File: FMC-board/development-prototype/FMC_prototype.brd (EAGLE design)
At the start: 103.9 x 69.8 mm, 91 parts, among them J1 PJ-102AH, J2 DC_POWER_JACK-PJ-102AH, U1 TPS79301, U10 ADN4664, U11 ADN4663, U2 TPS79333, U3 ADN4663, U4 ADN4663, U5 ADN4664, U6 PDS1-S12-S5-S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

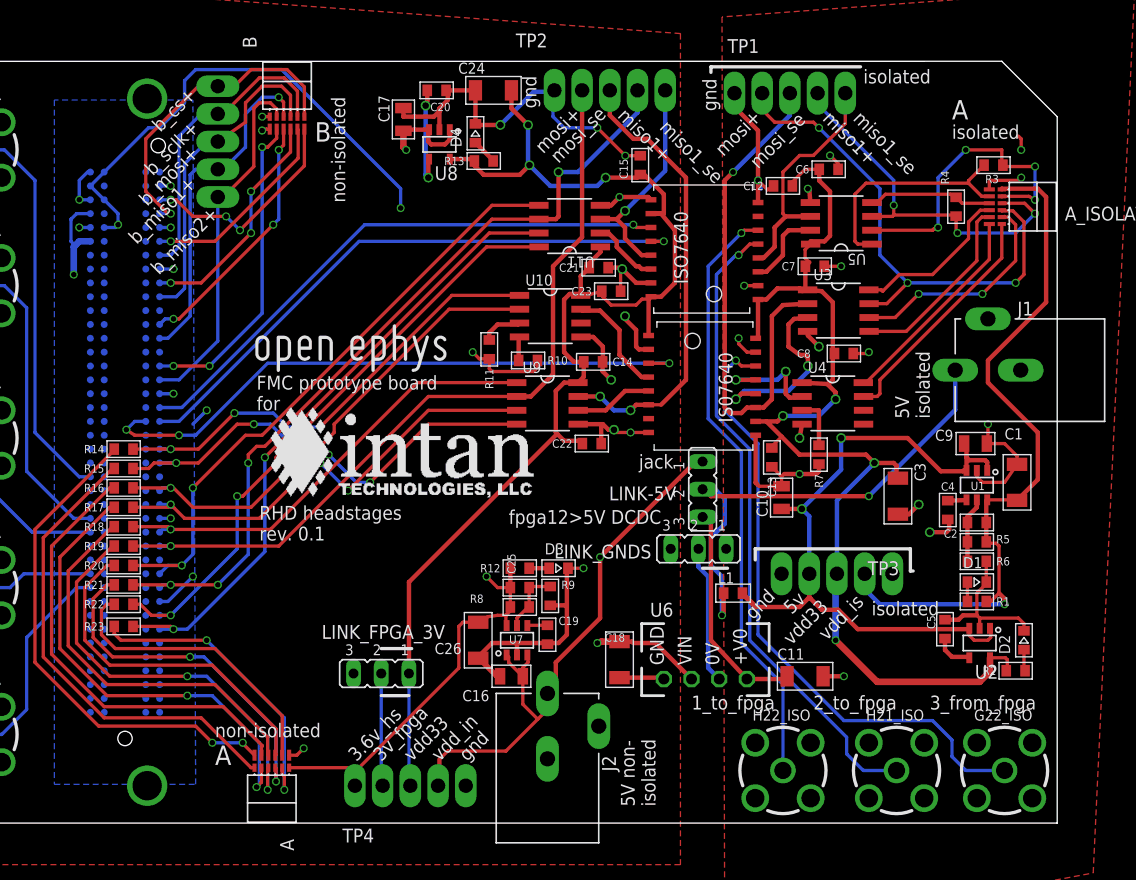
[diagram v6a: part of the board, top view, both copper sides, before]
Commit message: fixed some name and value labels
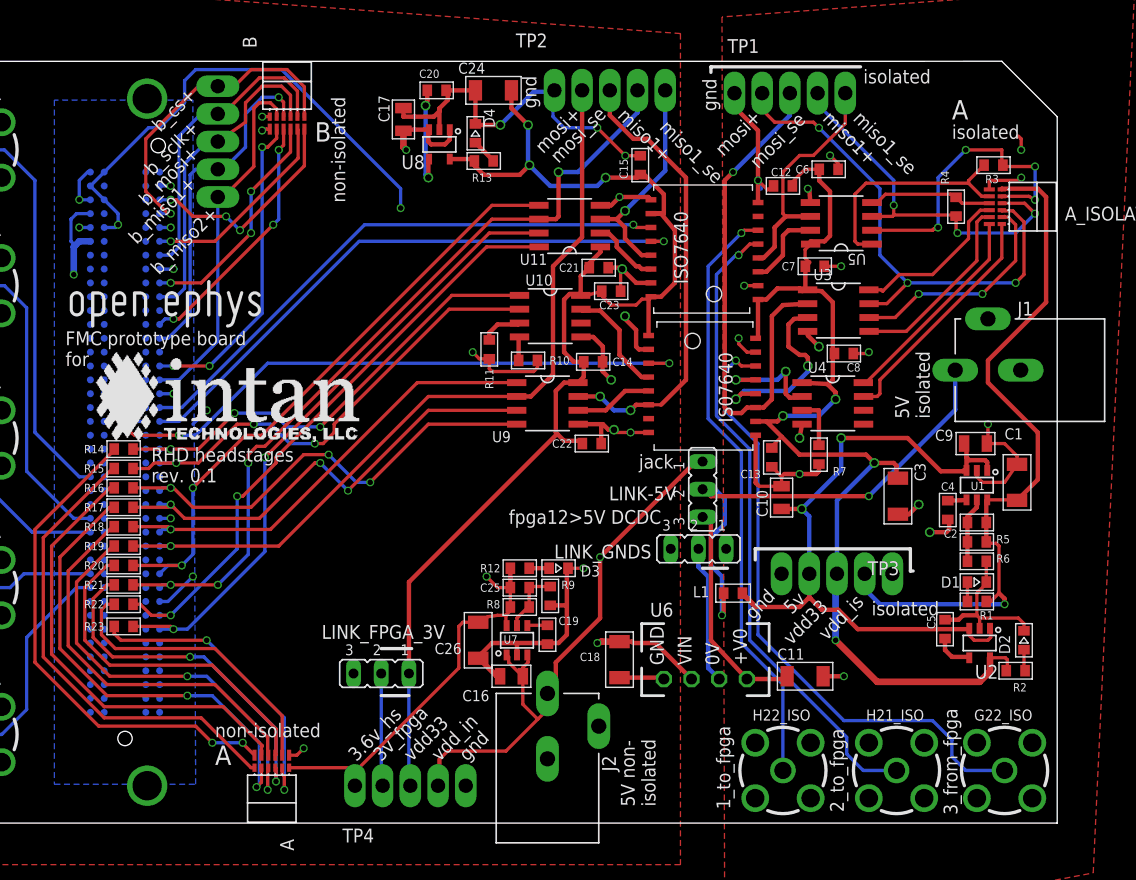
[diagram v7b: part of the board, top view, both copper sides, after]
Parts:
- moved U$1 17.5 mm to (12.7, 45.0)
- moved U$16 16.8 mm to (15.2, 34.3)

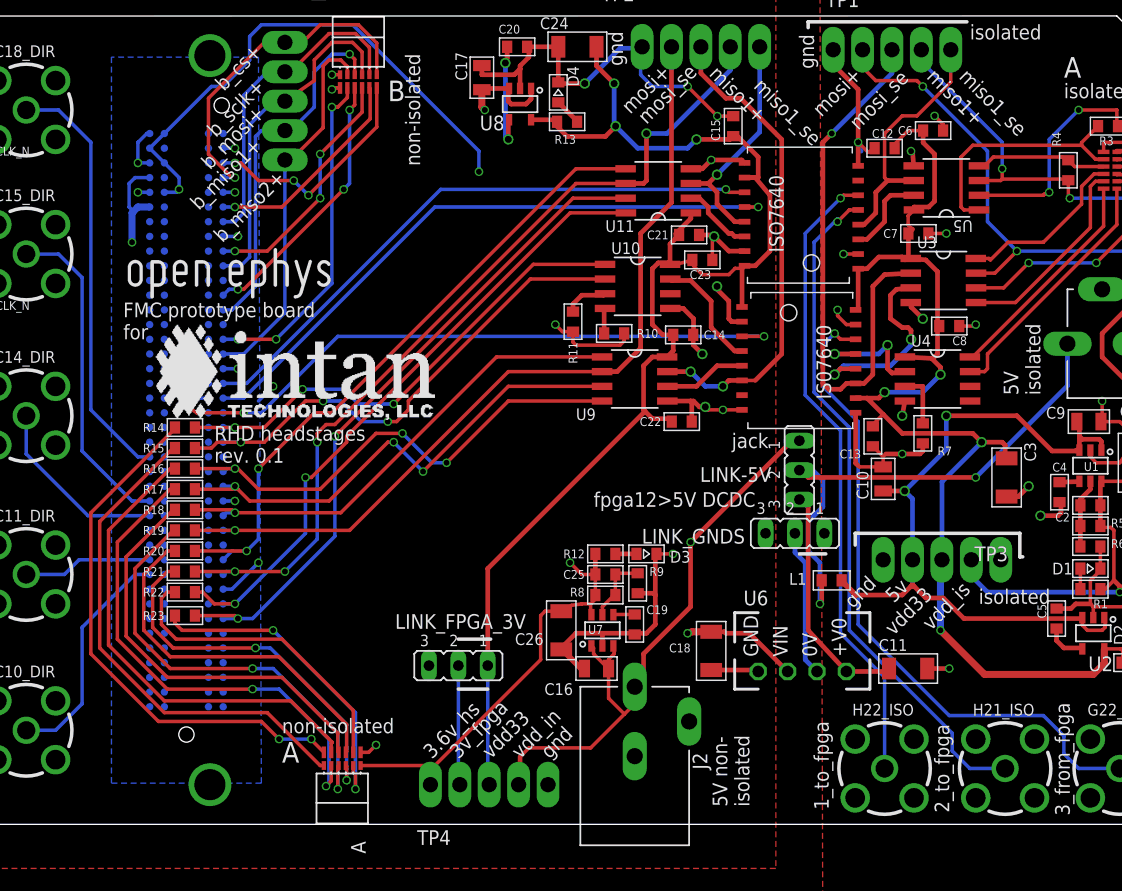
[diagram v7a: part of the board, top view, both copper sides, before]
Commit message: added labels to testpoints
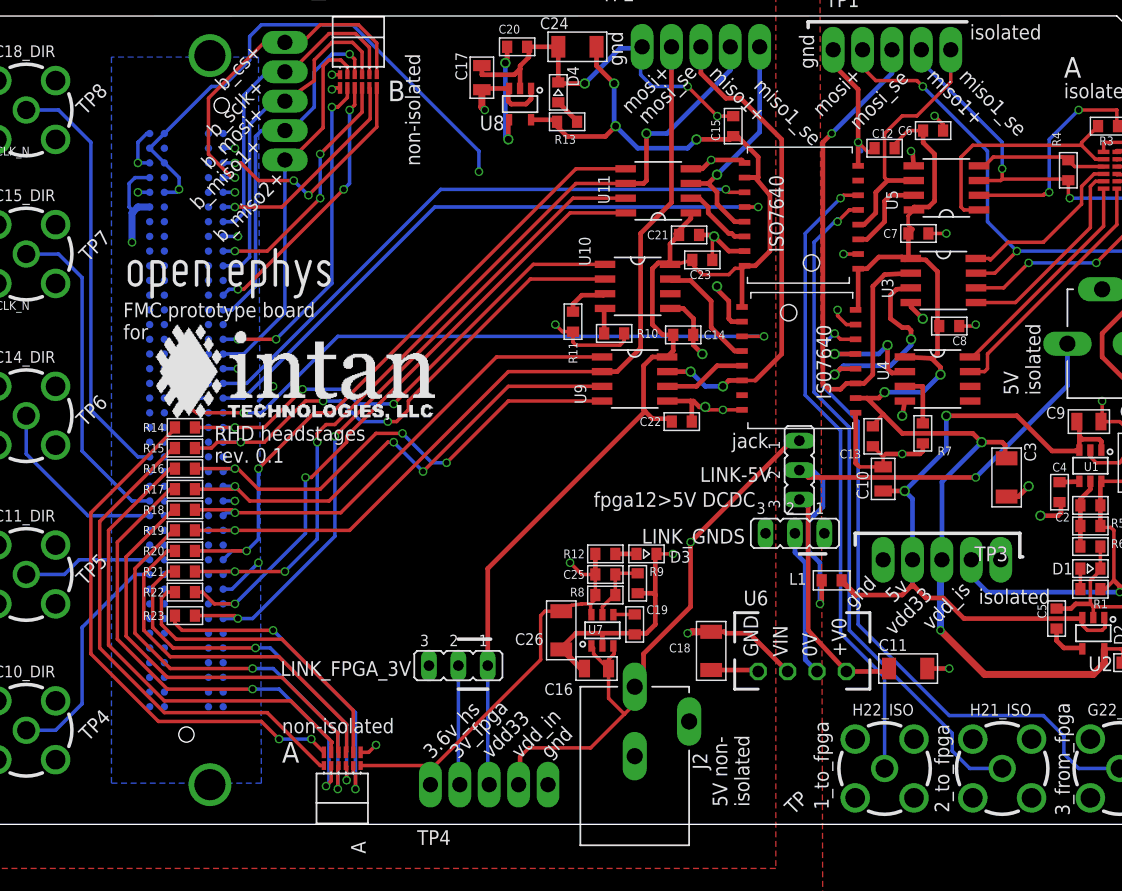
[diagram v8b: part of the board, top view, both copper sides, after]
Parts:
- moved H21_ISO 0.25 mm to (88.9, 4.83)
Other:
- board text added: "TP"
- board text added: "TP4"
- board text added: "TP5"
- board text added: "TP6"
- board text added: "TP7"
- board text added: "TP8"
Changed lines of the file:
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@@
 <grid distance="0.01" unitdist="inch" unit="inch" style="lines" multiple="1" display="yes" altdistance="0.0125" altunitdist="inch" altunit="inch"/>
 <layers>
-<layer number="1" name="Top" color="4" fill="1" visible="no" active="yes"/>
+<layer number="1" name="Top" color="4" fill="1" visible="yes" active="yes"/>
 <layer number="2" name="$GND" color="2" fill="1" visible="no" active="yes"/>
 <layer number="3" name="Route3" color="4" fill="3" visible="no" active="no"/>
@@
 <text x="53.594" y="27.432" size="1.27" layer="25" font="vector" ratio="15">fpga12&gt;5V DCDC</text>
 <rectangle x1="20.828" y1="20.066" x2="47.244" y2="29.972" layer="51"/>
+<text x="9.906" y="7.112" size="1.27" layer="25" font="vector" ratio="15" rot="R45">TP4</text>
+<text x="9.652" y="20.574" size="1.27" layer="25" font="vector" ratio="15" rot="R45">TP5</text>
+<text x="9.652" y="34.29" size="1.27" layer="25" font="vector" ratio="15" rot="R45">TP6</text>
+<text x="9.906" y="48.514" size="1.27" layer="25" font="vector" ratio="15" rot="R45">TP7</text>
+<text x="9.652" y="61.214" size="1.27" layer="25" font="vector" ratio="15" rot="R45">TP8</text>
+<text x="70.866" y="0.762" size="1.27" layer="25" font="vector" ratio="15" rot="R45">TP</text>
 </plain>
 <attributes>
@@
 <element name="U$1" library="open-ephys" package="OPEN_EPHYS_LOGO" value="OPEN_EPHYS_LOGO" x="12.7" y="44.958"/>
 <element name="U11" library="jonnew" package="SOIC127P500X400-8N" value="ADN4663" x="59.182" y="54.737" smashed="yes" rot="R180">
-<attribute name="NAME" x="54.61" y="51.181" size="1.016" layer="25" font="vector" ratio="18" rot="SR0"/>
+<attribute name="NAME" x="54.991" y="53.594" size="1.016" layer="25" font="vector" ratio="18" rot="SR90"/>
 <attribute name="VALUE" x="61.976" y="58.547" size="1.016" layer="27" font="vector" ratio="18" rot="SR180"/>
 </element>
 <element name="U5" library="jonnew" package="SOIC127P500X400-8N" value="ADN4664" x="84.074" y="54.991" smashed="yes" rot="R180">
-<attribute name="NAME" x="86.36" y="52.197" size="1.016" layer="25" font="vector" ratio="18" rot="SR180"/>
+<attribute name="NAME" x="79.883" y="53.086" size="1.016" layer="25" font="vector" ratio="18" rot="SR90"/>
 <attribute name="VALUE" x="88.011" y="56.134" size="1.016" layer="27" font="vector" ratio="18" rot="SR270"/>
 </element>
 <element name="U3" library="jonnew" package="SOIC127P500X400-8N" value="ADN4663" x="83.82" y="46.99" smashed="yes">
-<attribute name="NAME" x="81.534" y="49.784" size="1.016" layer="25" font="vector" ratio="18" rot="SR0"/>
+<attribute name="NAME" x="79.502" y="45.466" size="1.016" layer="25" font="vector" ratio="18" rot="SR90"/>
 <attribute name="VALUE" x="88.9" y="42.672" size="1.016" layer="27" font="vector" ratio="18" rot="SR90"/>
 </element>
 <element name="U4" library="jonnew" package="SOIC127P500X400-8N" value="ADN4663" x="83.312" y="38.481" smashed="yes">
-<attribute name="NAME" x="81.026" y="41.275" size="1.016" layer="25" font="vector" ratio="18" rot="SR0"/>
+<attribute name="NAME" x="79.121" y="38.354" size="1.016" layer="25" font="vector" ratio="18" rot="SR90"/>
 <attribute name="VALUE" x="83.058" y="34.925" size="1.016" layer="27" font="vector" ratio="18" rot="SR0"/>
 </element>
 <element name="U9" library="jonnew" package="SOIC127P500X400-8N" value="ADN4664" x="57.15" y="38.481" smashed="yes">
-<attribute name="NAME" x="52.07" y="34.925" size="1.016" layer="25" font="vector" ratio="18" rot="SR0"/>
+<attribute name="NAME" x="52.959" y="36.322" size="1.016" layer="25" font="vector" ratio="18" rot="SR90"/>
 <attribute name="VALUE" x="54.356" y="34.671" size="1.016" layer="27" font="vector" ratio="18" rot="SR0"/>
 </element>
 <element name="U10" library="jonnew" package="SOIC127P500X400-8N" value="ADN4664" x="57.404" y="46.482" smashed="yes">
-<attribute name="NAME" x="55.118" y="49.276" size="1.016" layer="25" font="vector" ratio="18" rot="SR0"/>
+<attribute name="NAME" x="53.34" y="48.26" size="1.016" layer="25" font="vector" ratio="18" rot="SR90"/>
 <attribute name="VALUE" x="58.928" y="43.688" size="1.016" layer="27" font="vector" ratio="18" rot="SR90"/>
 </element>
@@
 </element>
 <element name="LINK_FPGA_3V" library="jumper" package="JP2" value="" x="41.91" y="13.716" smashed="yes" rot="R180">
-<attribute name="NAME" x="47.752" y="18.161" size="1.27" layer="25" ratio="10" rot="R180"/>
+<attribute name="NAME" x="37.846" y="14.097" size="1.27" layer="25" ratio="10" rot="R180"/>
 <attribute name="VALUE" x="45.466" y="18.034" size="1.27" layer="27" ratio="10" rot="R180"/>
 </element>
@@
 <element name="C15_DIR" library="jonnew" package="SMA_JACK_142-0701-201" value="142-0701" x="4.572" y="49.276"/>
 <element name="C18_DIR" library="jonnew" package="SMA_JACK_142-0701-201" value="142-0701" x="4.572" y="61.722"/>
-<element name="H21_ISO" library="jonnew" package="SMA_JACK_142-0701-201" value="142-0701" x="89.154" y="4.826"/>
+<element name="H21_ISO" library="jonnew" package="SMA_JACK_142-0701-201" value="142-0701" x="88.9" y="4.826"/>
 <element name="H22_ISO" library="jonnew" package="SMA_JACK_142-0701-201" value="142-0701" x="78.74" y="4.826"/>
 <element name="G22_ISO" library="jonnew" package="SMA_JACK_142-0701-201" value="142-0701" x="99.06" y="4.826"/>
@@
 <wire x1="84.582" y1="7.874" x2="84.582" y2="6.35" width="0.3048" layer="16"/>
 <wire x1="84.582" y1="6.35" x2="86.106" y2="4.826" width="0.3048" layer="16"/>
-<wire x1="86.106" y1="4.826" x2="89.154" y2="4.826" width="0.3048" layer="16"/>
+<wire x1="86.106" y1="4.826" x2="88.9" y2="4.826" width="0.3048" layer="16"/>
 </signal>
 <signal name="TP2_FROM_SMA">
